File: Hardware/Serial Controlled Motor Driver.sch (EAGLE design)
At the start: 46 parts, among them J1 DNP, J2 DNP, J3 DNP, J4 DNP, J5 DNP, J6 DNP, J8 CORTEX_DEBUGPTH, U1 CY8C4245LQI-483, U2 DRV8835

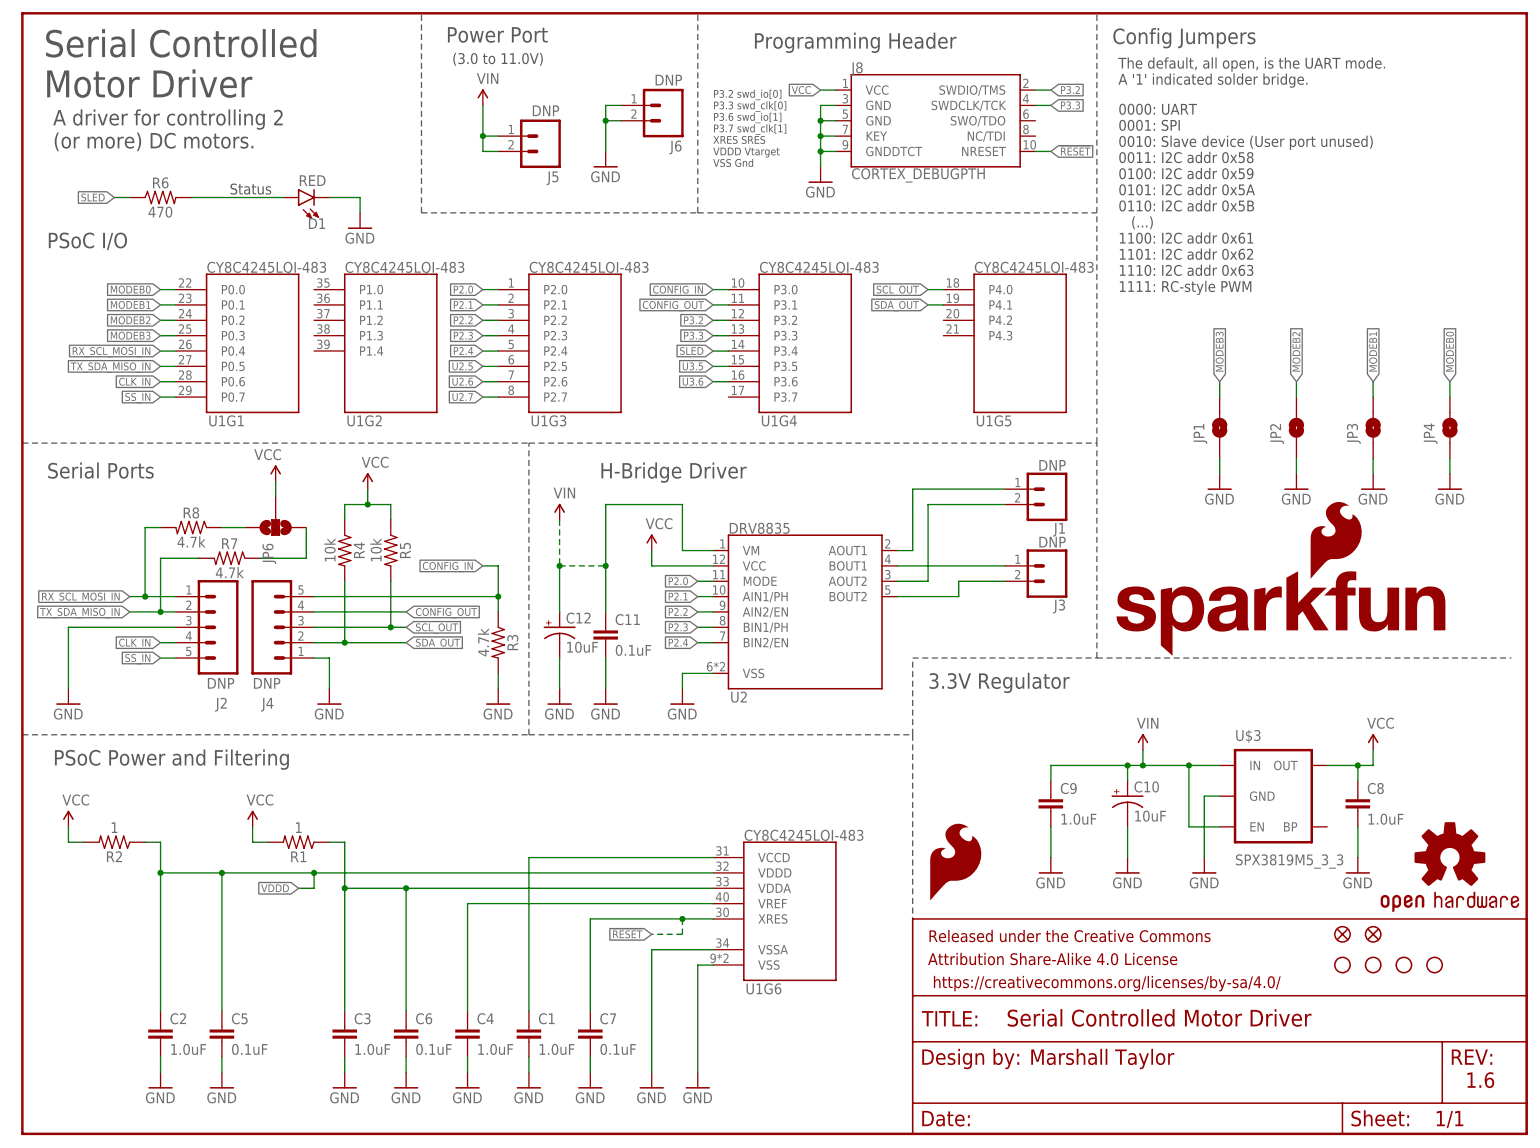
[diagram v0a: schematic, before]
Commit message: Prepping for QC, tuning gitignores
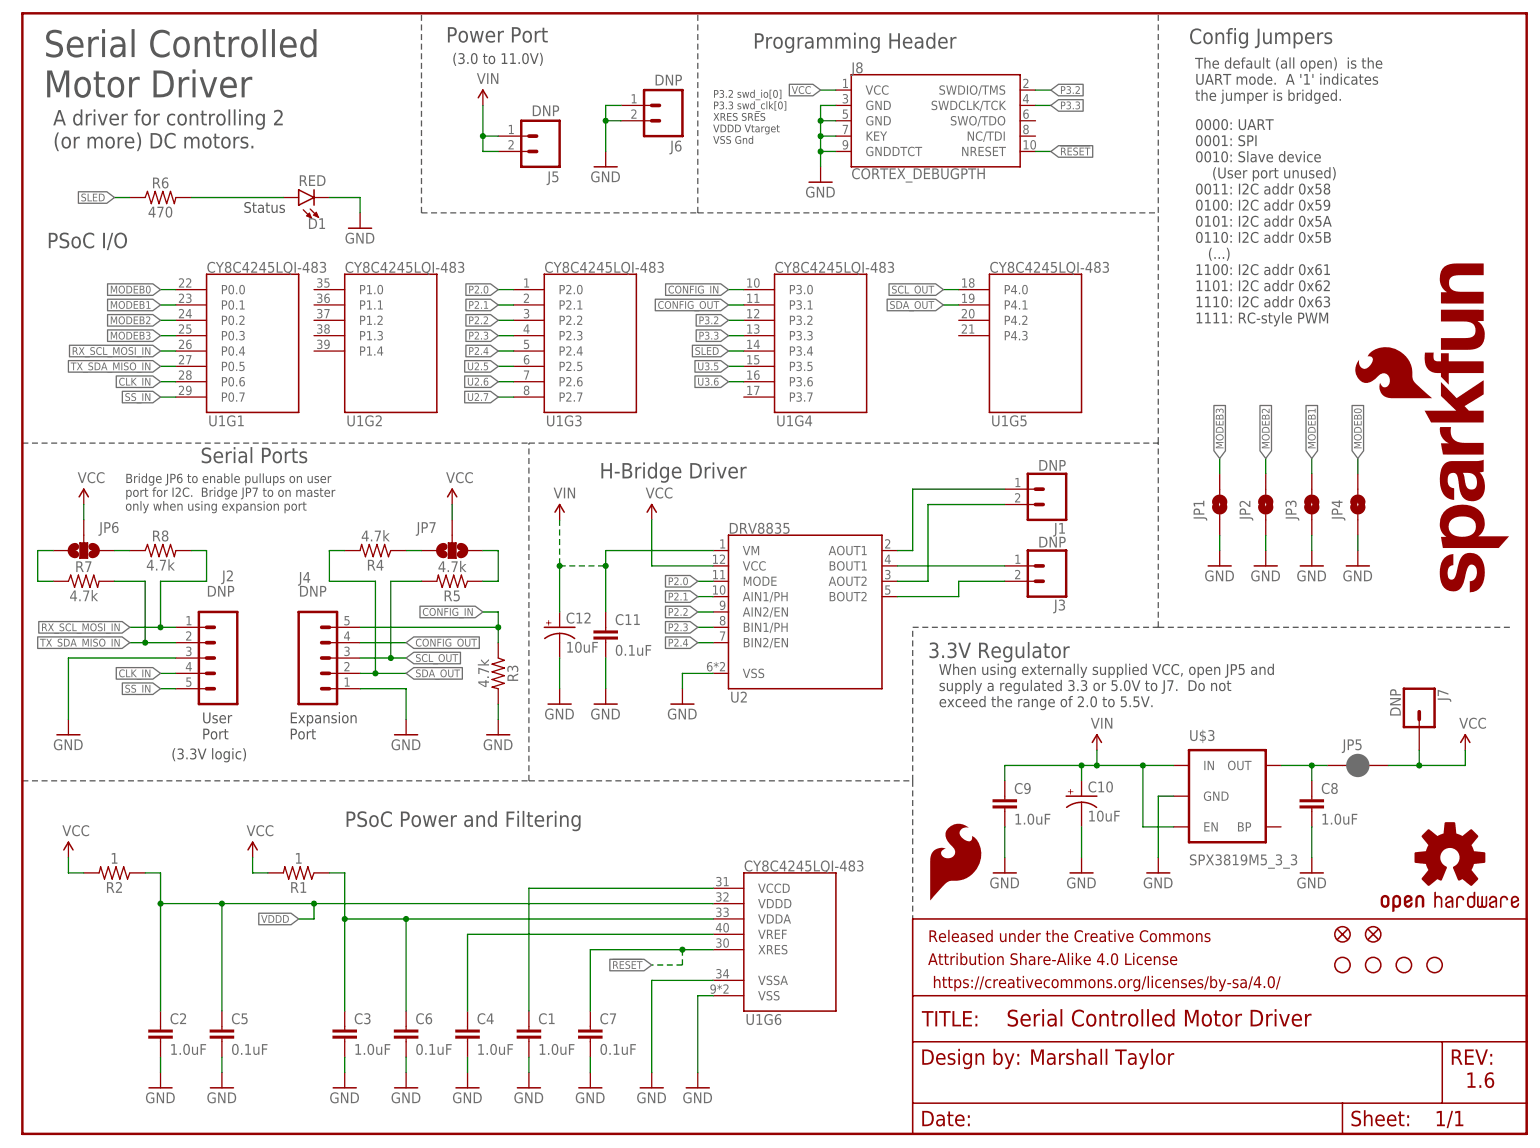
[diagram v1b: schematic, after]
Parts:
- added J7: DNP, SparkFun-Connectors:CONN_01PTH
- added JP5: JUMPER-PAD-2, SparkFun-Jumpers:JUMPER-PAD-2-NC_BY_PASTE
- added JP7: JUMPER-PAD-3-NOYES_SILK, SparkFun-Passives:JUMPER-PAD-3-NOYES_SILK
- R4, R5: value 10k -> 4.7k; device SparkFun-Resistors:10KOHM-0603-1/10W-1% -> SparkFun-Resistors:4.7KOHM-0603-1/10W-1%
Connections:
- new net N$2: JP7.1, R4.1
- new net N$5: C8.1, JP5.1, U$3.OUT
- new net N$6: JP7.3, R5.1
- net VCC: now also J7.1, JP5.2, JP7.2; no longer C8.1, R4.1, R5.1, U$3.OUT
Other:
- note added: "(3.3V logic)"
- note added: "Bridge JP6 to enable pullups on user port for I2C. Bridge JP7 to on master only when using expansion port"
- note added: "Expansion Port"
- note added: "P3.2 swd_io[0] P3.3 swd_clk[0] XRES SRES VDDD Vtarget VSS Gnd"
- note added: "The default (all open) is the UART mode. A '1' indicates the jumper is bridged."
- note added: "User Port"
- note added: "When using externally supplied VCC, open JP5 and supply a regulated 3.3 or 5.0V to J7. Do not exceed the range of 2.0 to 5.5V."
- note removed: "P3.2 swd_io[0] P3.3 swd_clk[0] P3.6 swd_io[1] P3.7 swd_clk[1] XRES SRES VDDD Vtarget VSS Gnd"
- note removed: "The default, all open, is the UART mode. A '1' indicated solder bridge."
- moved on the sheet: C10, C8, C9, J2, J4, JP1, JP2, JP3, JP4, JP6, R1, R2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
